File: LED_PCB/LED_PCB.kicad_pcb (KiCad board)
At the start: 2 copper layers, 132.4 x 152.3 mm, 125 parts, among them J1 TEST_1P, J10 TEST_1P, J11 TEST_1P, J12 TEST_1P, J13 TEST_1P, J2 TEST_1P, J3 TEST_1P, J4 TEST_1P, J5 TEST_1P, J6 TEST_1P, J7 TEST_1P, J8 TEST_1P, J9 Conn_01x06, Q1 Q_NMOS_GSD, Q2 Q_PMOS_GDS, Q3 Q_NMOS_SDG, U1 MIC5233-3.3YS-TR, U2 ATTINY85-20SU

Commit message: Finished layout and created gerbers.
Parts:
- added REF**: VIA_12_22, CustomFootprints:VIA_12_22, F.Cu at (181.6, 143.5)
- added REF**: VIA_12_22, CustomFootprints:VIA_12_22, F.Cu at (207.0, 116.8)
- added REF**: VIA_12_22, CustomFootprints:VIA_12_22, F.Cu at (207.0, 115.6)
- added REF**: VIA_12_22, CustomFootprints:VIA_12_22, F.Cu at (193.0, 61.0)
- added REF**: VIA_12_22, CustomFootprints:VIA_12_22, F.Cu at (193.0, 62.2)
- added REF**: VIA_12_22, CustomFootprints:VIA_12_22, F.Cu at (191.8, 62.2)
- added REF**: VIA_12_22, CustomFootprints:VIA_12_22, F.Cu at (191.8, 61.0)
- added REF**: VIA_12_22, CustomFootprints:VIA_12_22, F.Cu at (165.1, 45.7)
- added REF**: VIA_12_22, CustomFootprints:VIA_12_22, F.Cu at (166.4, 45.7)
- added REF**: VIA_12_22, CustomFootprints:VIA_12_22, F.Cu at (165.1, 47.0)
- added REF**: VIA_12_22, CustomFootprints:VIA_12_22, F.Cu at (154.9, 48.3)
- added REF**: VIA_12_22, CustomFootprints:VIA_12_22, F.Cu at (182.9, 143.5)
- added REF**: VIA_12_22, CustomFootprints:VIA_12_22, F.Cu at (154.9, 49.5)
- added REF**: VIA_12_22, CustomFootprints:VIA_12_22, F.Cu at (156.2, 49.5)
- added REF**: VIA_12_22, CustomFootprints:VIA_12_22, F.Cu at (156.2, 48.3)
- added REF**: VIA_12_22, CustomFootprints:VIA_12_22, F.Cu at (101.6, 63.5)
- added REF**: VIA_12_22, CustomFootprints:VIA_12_22, F.Cu at (101.6, 62.2)
- added REF**: VIA_12_22, CustomFootprints:VIA_12_22, F.Cu at (101.6, 61.0)
- added REF**: VIA_12_22, CustomFootprints:VIA_12_22, F.Cu at (86.4, 86.4)
- added REF**: VIA_12_22, CustomFootprints:VIA_12_22, F.Cu at (86.4, 87.6)
- added REF**: VIA_12_22, CustomFootprints:VIA_12_22, F.Cu at (87.6, 87.6)
- added REF**: VIA_12_22, CustomFootprints:VIA_12_22, F.Cu at (87.6, 86.4)
- added REF**: VIA_12_22, CustomFootprints:VIA_12_22, F.Cu at (182.9, 142.2)
- added REF**: VIA_12_22, CustomFootprints:VIA_12_22, F.Cu at (106.7, 147.3)
- added REF**: VIA_12_22, CustomFootprints:VIA_12_22, F.Cu at (106.7, 146.1)
- added REF**: VIA_12_22, CustomFootprints:VIA_12_22, F.Cu at (108.0, 147.3)
- added REF**: VIA_12_22, CustomFootprints:VIA_12_22, F.Cu at (108.0, 146.1)
- added REF**: VIA_12_22, CustomFootprints:VIA_12_22, F.Cu at (138.4, 156.2)
- added REF**: VIA_12_22, CustomFootprints:VIA_12_22, F.Cu at (138.4, 157.5)
- added REF**: VIA_12_22, CustomFootprints:VIA_12_22, F.Cu at (137.2, 157.5)
- added REF**: VIA_12_22, CustomFootprints:VIA_12_22, F.Cu at (137.2, 156.2)
- added REF**: VIA_12_22, CustomFootprints:VIA_12_22, F.Cu at (127.0, 156.2)
- added REF**: VIA_12_22, CustomFootprints:VIA_12_22, F.Cu at (127.0, 157.5)
- added REF**: VIA_12_22, CustomFootprints:VIA_12_22, F.Cu at (193.0, 143.5)
- added REF**: VIA_12_22, CustomFootprints:VIA_12_22, F.Cu at (128.3, 157.5)
- added REF**: VIA_12_22, CustomFootprints:VIA_12_22, F.Cu at (128.3, 156.2)
- added REF**: VIA_12_22, CustomFootprints:VIA_12_22, F.Cu at (191.8, 143.5)
- added REF**: VIA_12_22, CustomFootprints:VIA_12_22, F.Cu at (193.0, 142.2)
- added REF**: VIA_12_22, CustomFootprints:VIA_12_22, F.Cu at (191.8, 142.2)
- added REF**: VIA_12_22, CustomFootprints:VIA_12_22, F.Cu at (208.3, 116.8)
- added REF**: VIA_12_22, CustomFootprints:VIA_12_22, F.Cu at (208.3, 115.6)
- renumbered J4 to DIN, J10 to DIN, J11 to DOUT, J2 to GND, J3 to GND, J12 to RGB_EN, J6 to VCC, J7 to VDD, J1 to VIN, J5 to VIN, J13 to VIN_ADC, J8 to WHT_EN
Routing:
- net Net-(D8-Pad1): track 4.50 -> 10.1 mm
- net Net-(C1-Pad1): track 56.9 -> 61.7 mm
- net Net-(LED8-Pad2): track 31.2 -> 31.8 mm
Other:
- board text added: "1 VCC"
- board text added: "2 GND"
- board text added: "3 PB2"
- board text added: "4 PB1"
- board text added: "5 PB0"
- board text added: "6 PB5"
- board text added: "DIN"
- board text added: "DOUT"
- board text added: "LED_PCB Rev01"
- board text added: "RGB_EN"
- board text added: "RST"

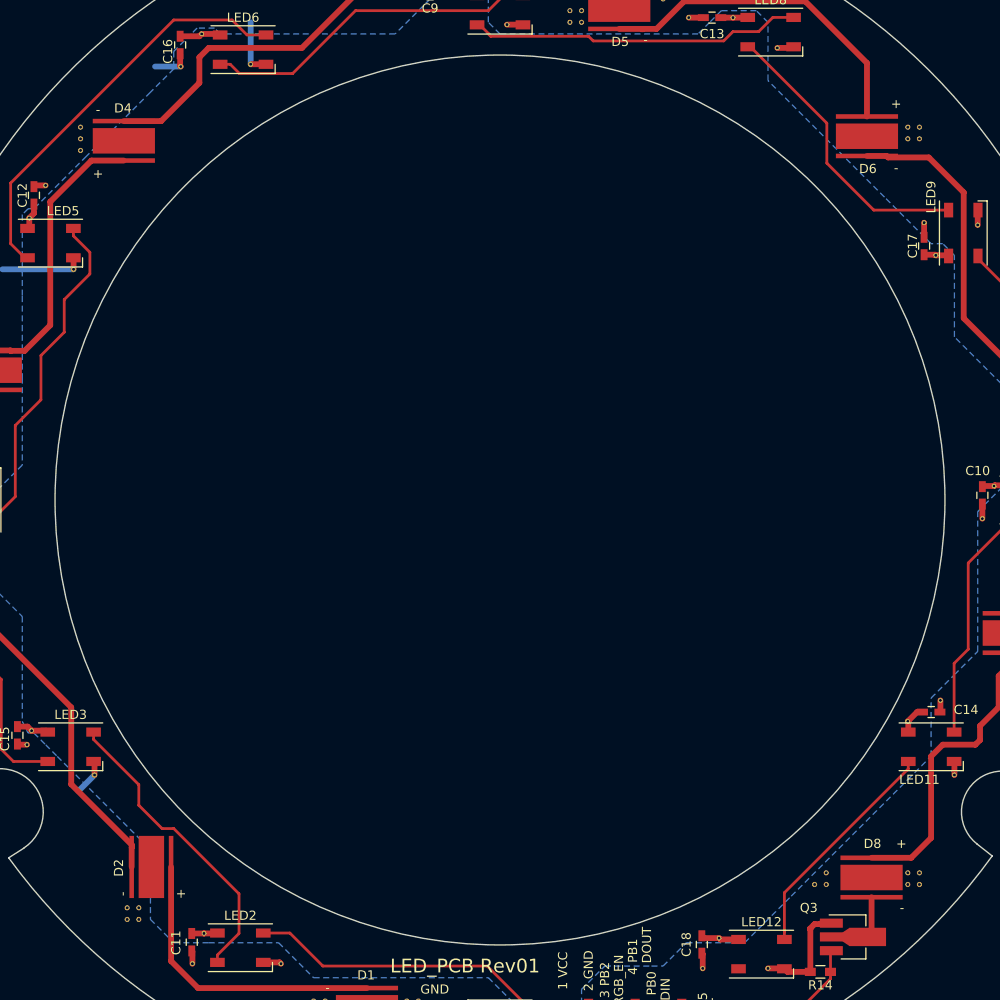
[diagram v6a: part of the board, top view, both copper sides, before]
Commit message: Updated layout to add giant mounting hole for center opening; ordered PCB's with this design.
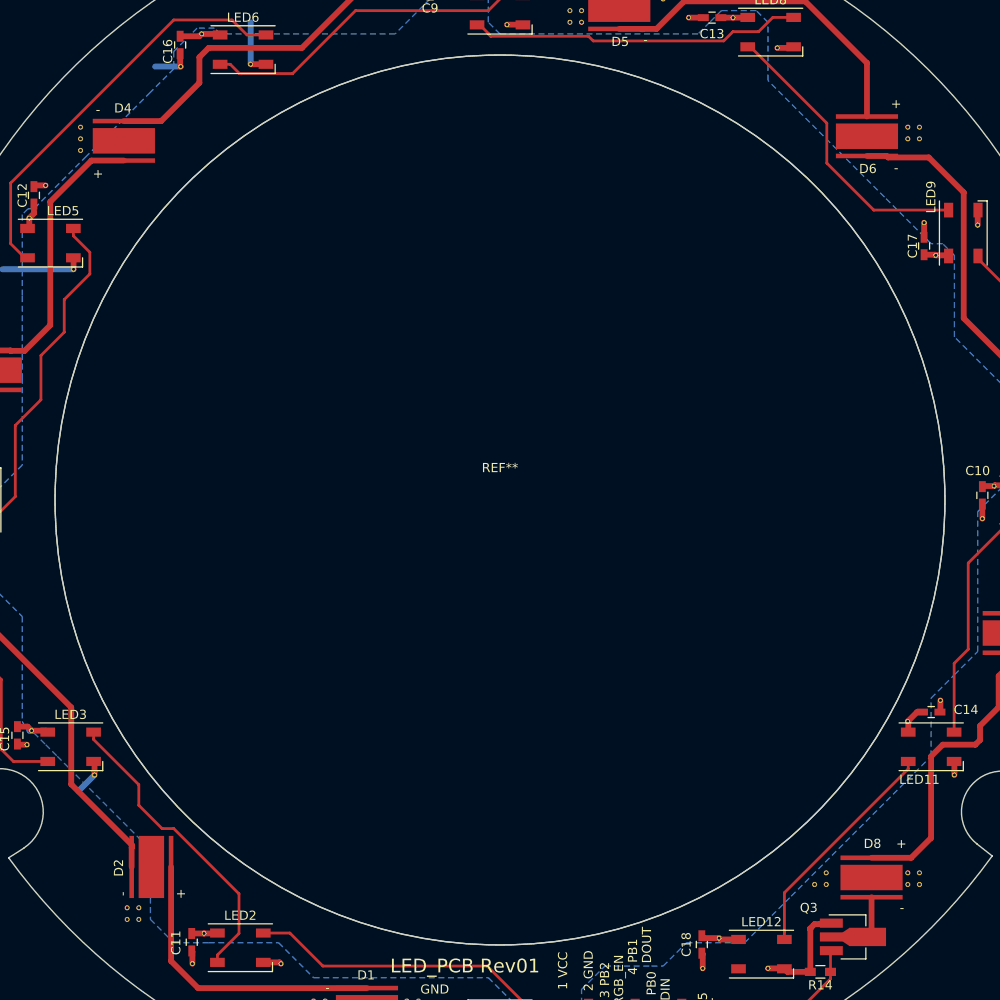
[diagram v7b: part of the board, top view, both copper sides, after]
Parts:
- added REF**: MountingHole_2.5mm, Mounting_Holes:MountingHole_2.5mm, F.Cu at (147.3, 101.6)
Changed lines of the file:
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@@
     (tracks 454)
     (zones 0)
-    (modules 166)
+    (modules 167)
     (nets 39)
   )
@@
     (mod_text_size 1 1)
     (mod_text_width 0.15)
-    (pad_size 0.5588 0.5588)
-    (pad_drill 0.3048)
+    (pad_size 97 97)
+    (pad_drill 97)
     (pad_to_mask_clearance 0.2)
     (aux_axis_origin 147.32 101.6)
@@
     (visible_elements 7FFEFF7F)
     (pcbplotparams
-      (layerselection 0x00020_00000000)
+      (layerselection 0x010e0_80000001)
       (usegerberextensions false)
       (excludeedgelayer true)
@@
       (net 2 GND))
   )
+  (module Mounting_Holes:MountingHole_2.5mm (layer F.Cu)
+    (at 147.32 101.6)
+    (descr "Mounting Hole 2.5mm, no annular")
+    (tags "mounting hole 2.5mm no annular")
+    (fp_text reference REF** (at 0 -3.5) (layer F.SilkS)
+      (effects (font (size 1 1) (thickness 0.15)))
+    )
+    (fp_text value MountingHole_2.5mm (at 0 3.5) (layer F.Fab)
+      (effects (font (size 1 1) (thickness 0.15)))
+    )
+    (fp_circle (center 0 0) (end 2.5 0) (layer Cmts.User) (width 0.15))
+    (fp_circle (center 0 0) (end 2.75 0) (layer F.CrtYd) (width 0.05))
+    (pad "" np_thru_hole circle (at 0 0) (size 97 97) (drill 97) (layers *.Cu *.Mask))
+  )
   (gr_text "LED_PCB Rev01" (at 143.51 152.4) (layer F.SilkS)
